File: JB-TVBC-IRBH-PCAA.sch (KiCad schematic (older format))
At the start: 11 parts, among them J1 CONN_2x20_FEM_100PITCH_635INS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, U1 CAT24C32

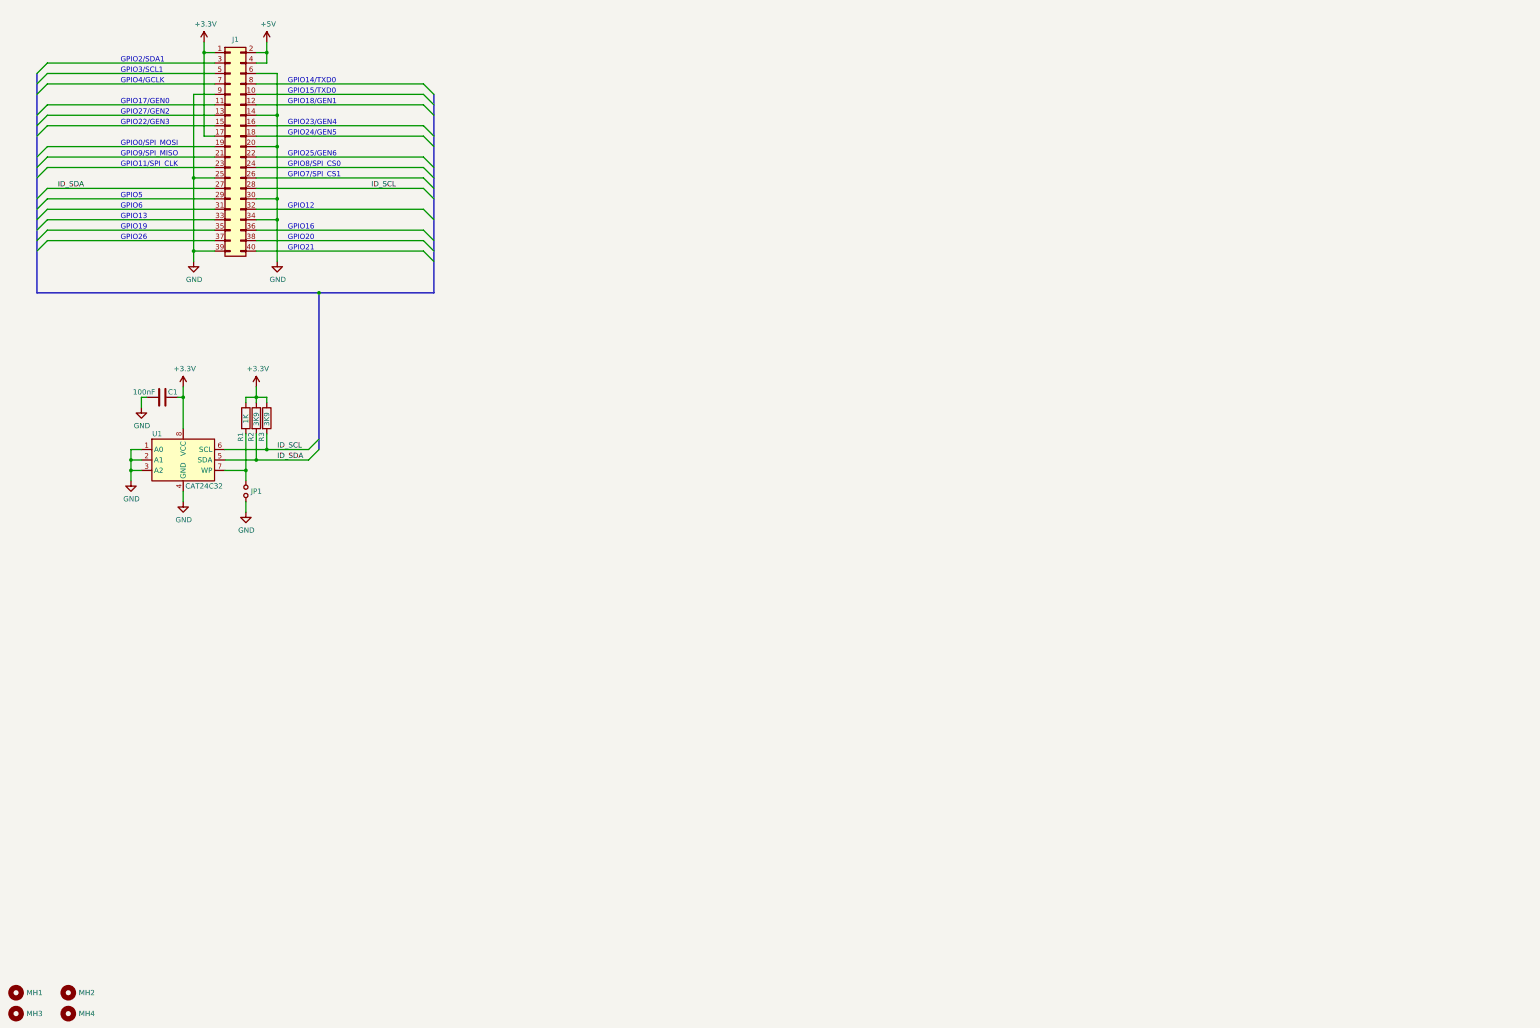
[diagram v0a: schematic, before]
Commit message: WIP. need to remove pull-up on PHASE and add pull-down on IN (gate driver
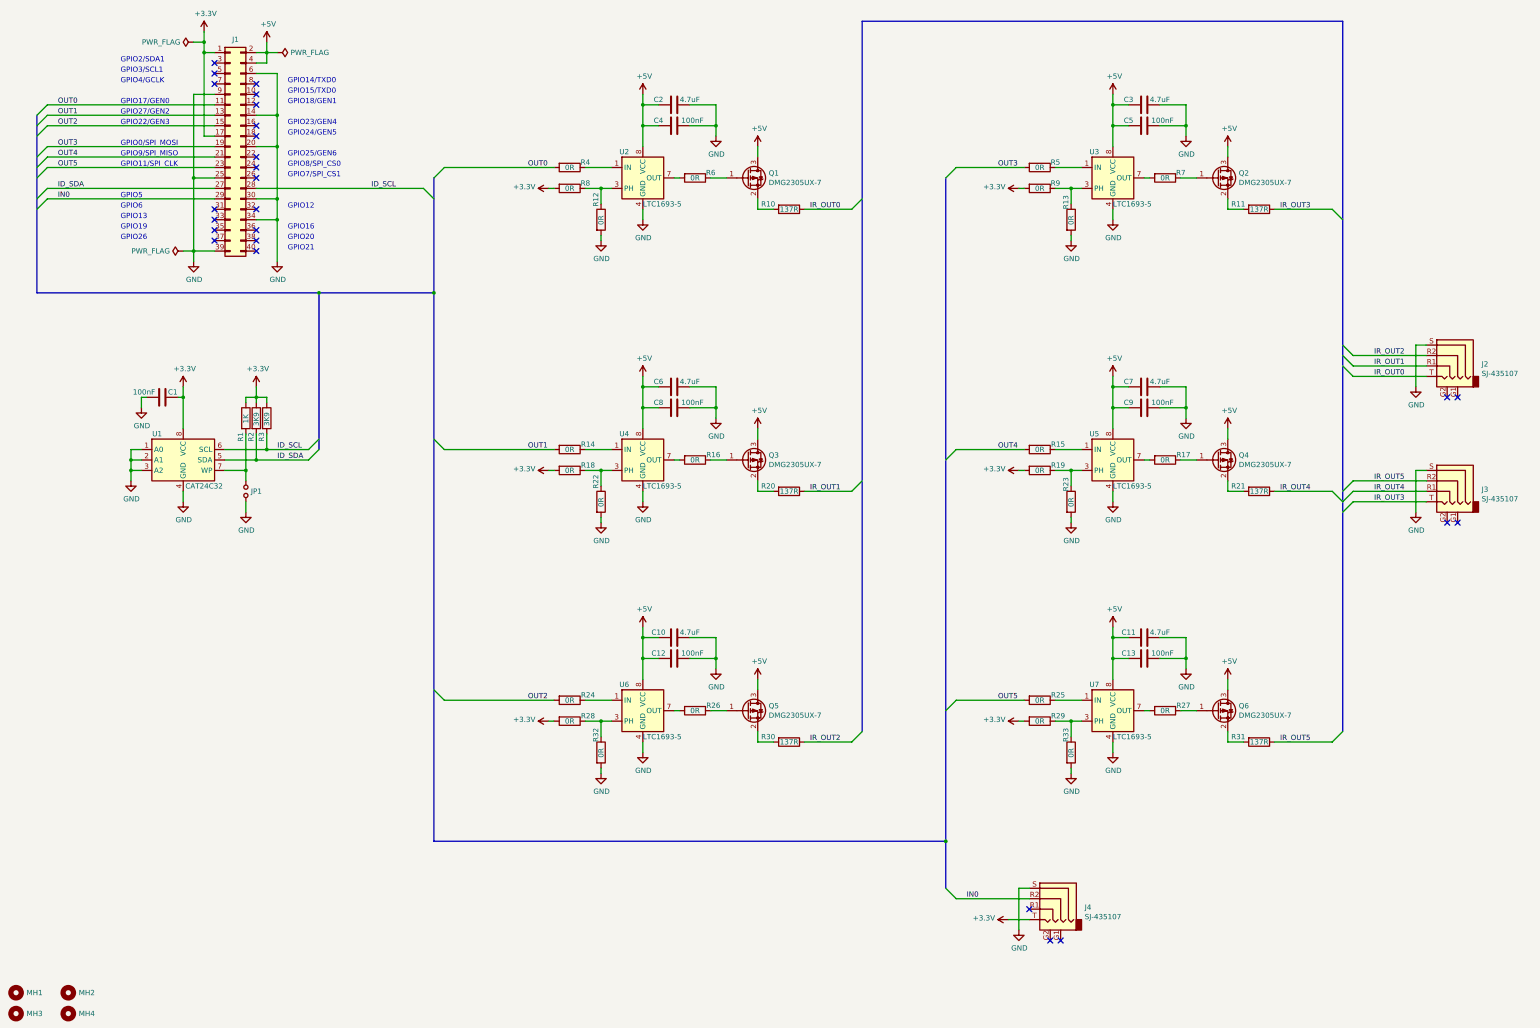
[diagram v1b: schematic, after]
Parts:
- removed C1: 100nF_0603_50V, Capacitor_SMD:C_0603_1608Metric_Pad1.05x0.95mm_HandSolder, symbol JB_Cap_Smd_50v:100nF_0603_50V
- added C1, C12, C13, C4, C5, C8, C9: 100nF_CER_0603_50V, Capacitor_SMD:C_0603_1608Metric_Pad1.05x0.95mm_HandSolder, symbol JB_Cap_Smd_50v:100nF_CER_0603_50V
- added C10, C11, C2, C3, C6, C7: 4.7uF_CER_0805_16V, Capacitor_SMD:C_0805_2012Metric_Pad1.15x1.40mm_HandSolder, symbol JB_Cap_Smd_16v:4.7uF_CER_0805_16V
- added J2, J3, J4: SJ-435107, JB_Connector_Barrel_Audio:SJ-435107, symbol JB_Connector_Barrel_Audio:SJ-435107
- added Q1, Q2, Q3, Q4, Q5, Q6: DMG2305UX-7, Package_TO_SOT_SMD:SOT-23_Handsoldering, symbol JB_Mosfet_P-Ch:DMG2305UX-7
- added R10, R11, R20, R21, R30, R31: 137R_1206_250MW, Resistor_SMD:R_1206_3216Metric_Pad1.42x1.75mm_HandSolder, symbol JB_Res_Smd_0w250:137R_1206_250MW
- added R12, R13, R14, R15, R16, R17, R18, R19, R22, R23, R24, R25, R26, R27, R28, R29, R32, R33, R4, R5, R6, R7, R8, R9: 0R_0603_100MW, Resistor_SMD:R_0603_1608Metric_Pad1.05x0.95mm_HandSolder, symbol JB_Res_Smd_0w100:0R_0603_100MW
- added U2, U3, U4, U5, U6, U7: LTC1693-5, Package_SO:MSOP-8_3x3mm_P0.65mm, symbol JB_Gate_Driver:LTC1693-5
- J1: Digi-Key PArt Number SAM9319-ND -> (none); Digi-Key Part Number (none) -> SAM9319-ND
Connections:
- net +3V3: now also C1.1, J4.T, R18.2, R19.2, R28.2, R29.2, R8.2, R9.2
- net +5V: now also C10.2, C11.2, C12.2, C13.2, C2.2, C3.2, C4.2, C5.2, C6.2, C7.2, C8.2, C9.2, Q1.3 (D), Q2.3 (D), Q3.3 (D), Q4.3 (D), Q5.3 (D), Q6.3 (D), U2.8 (VCC), U3.8 (VCC), U4.8 (VCC), U5.8 (VCC), U6.8 (VCC), U7.8 (VCC)
- net GND: now also C1.2, C10.1, C11.1, C12.1, C13.1, C2.1, C3.1, C4.1, C5.1, C6.1, C7.1, C8.1, C9.1, J2.S, J3.S, J4.S, R12.2, R13.2, R22.2, R23.2, R32.2, R33.2, U2.4 (GND), U3.4 (GND), U4.4 (GND), U5.4 (GND), U6.4 (GND), U7.4 (GND)
- net OUT0: now reaches J1.11 (Pin_11)
- net OUT0: now also R4.2
- net OUT1: now reaches J1.13 (Pin_13)
- net OUT1: now also R14.2
- net OUT2: now reaches J1.15 (Pin_15)
- net OUT2: now also R24.2
- net OUT3: now reaches J1.19 (Pin_19)
- net OUT3: now also R5.2
- net OUT4: now reaches J1.21 (Pin_21)
- net OUT4: now also R15.2
- net OUT5: now reaches J1.23 (Pin_23)
- net OUT5: now also R25.2
- net IN0: now reaches J1.29 (Pin_29)
- net IN0: now also J4.R2
- new net: R4.1, U2.1 (IN)
- new net: R12.1, R8.1, U2.3 (PH)
- new net: R6.2, U2.7 (OUT)
- new net: R14.1, U4.1 (IN)
- new net: R18.1, R22.1, U4.3 (PH)
- new net: R16.2, U4.7 (OUT)
- new net: R24.1, U6.1 (IN)
- new net: R28.1, R32.1, U6.3 (PH)
- new net: R26.2, U6.7 (OUT)
- new net: R5.1, U3.1 (IN)
- new net: R13.1, R9.1, U3.3 (PH)
- new net: R7.2, U3.7 (OUT)
- new net: R15.1, U5.1 (IN)
- new net: R19.1, R23.1, U5.3 (PH)
- new net: R17.2, U5.7 (OUT)
- new net: R25.1, U7.1 (IN)
- new net: R29.1, R33.1, U7.3 (PH)
- new net: R27.2, U7.7 (OUT)
- new net: Q1.1 (G), R6.1
- new net: Q2.1 (G), R7.1
- new net: Q4.1 (G), R17.1
- new net: Q6.1 (G), R27.1
- new net: Q5.1 (G), R26.1
- new net: Q3.1 (G), R16.1
- new net: Q1.2 (S), R10.2
- new net: Q2.2 (S), R11.2
- new net: Q4.2 (S), R21.2
- new net: Q3.2 (S), R20.2
- new net: Q5.2 (S), R30.2
- new net: Q6.2 (S), R31.2
- new net IR_OUT0: J2.T, R10.1
- new net IR_OUT1: J2.R1, R20.1
- new net IR_OUT2: J2.R2, R30.1
- new net IR_OUT3: J3.T, R11.1
- new net IR_OUT4: J3.R1, R21.1
- new net IR_OUT5: J3.R2, R31.1
- no-connect marks 0 -> 26

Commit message: adding fiducial + graphics symbol
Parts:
- added FID1, FID2, FID3, FID4, FID5, FID6, FID7, FID8: Fiducial, JB_Mechanical:Fiducial_1.5mm_Mask3mm, symbol JB_Mechanical:Fiducial
- added G1: JudeBake_Logo, JB_Bitmaps:JB_Logo_10MM, symbol JB_Bitmap:JudeBake_Logo
- added G2: CC-BY-SA_Logo, JB_Bitmaps:CC-BY-SA_10MM, symbol JB_Bitmap:CC-BY-SA_Logo
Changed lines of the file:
@@
 	0    1    1    0
+$EndComp
+$Comp
+L JB_Bitmap:JudeBake_Logo G1
+U 1 1 5E70CA7A
+P 15300 9000
+F 0 "G1" H 15300 8877 60  0001 C CNN
+F 1 "JudeBake_Logo" H 15300 9123 60  0001 C CNN
+F 2 "JB_Bitmaps:JB_Logo_10MM" H 15300 9000 50  0001 C CNN
+F 3 "" H 15300 9000 50  0001 C CNN
+	1    15300 9000
+	1    0    0    -1
+$EndComp
+$Comp
+L JB_Bitmap:CC-BY-SA_Logo G2
+U 1 1 5E70D851
+P 15800 9000
+F 0 "G2" H 15800 8955 60  0001 C CNN
+F 1 "CC-BY-SA_Logo" H 15800 9045 60  0001 C CNN
+F 2 "JB_Bitmaps:CC-BY-SA_10MM" H 15800 9000 50  0001 C CNN
+F 3 "" H 15800 9000 50  0001 C CNN
+	1    15800 9000
+	1    0    0    -1
+$EndComp
+$Comp
+L JB_Mechanical:Fiducial FID1
+U 1 1 5E715969
+P 1700 10200
+F 0 "FID1" H 1785 10200 50  0000 L CNN
+F 1 "Fiducial" H 1700 10325 50  0001 C CNN
+F 2 "JB_Mechanical:Fiducial_1.5mm_Mask3mm" H 1700 10200 50  0001 C CNN
+F 3 "~" H 1700 10200 50  0001 C CNN
+	1    1700 10200
+	1    0    0    -1
+$EndComp
+$Comp
+L JB_Mechanical:Fiducial FID3
+U 1 1 5E71703E
+P 1700 10400
+F 0 "FID3" H 1785 10400 50  0000 L CNN
+F 1 "Fiducial" H 1700 10525 50  0001 C CNN
+F 2 "JB_Mechanical:Fiducial_1.5mm_Mask3mm" H 1700 10400 50  0001 C CNN
+F 3 "~" H 1700 10400 50  0001 C CNN
+	1    1700 10400
+	1    0    0    -1
+$EndComp
+$Comp
+L JB_Mechanical:Fiducial FID4
+U 1 1 5E7179F8
+P 2200 10400
+F 0 "FID4" H 2285 10400 50  0000 L CNN
+F 1 "Fiducial" H 2200 10525 50  0001 C CNN
+F 2 "JB_Mechanical:Fiducial_1.5mm_Mask3mm" H 2200 10400 50  0001 C CNN
+F 3 "~" H 2200 10400 50  0001 C CNN
+	1    2200 10400
+	1    0    0    -1
+$EndComp
+$Comp
+L JB_Mechanical:Fiducial FID2
+U 1 1 5E7183BE
+P 2200 10200
+F 0 "FID2" H 2285 10200 50  0000 L CNN
+F 1 "Fiducial" H 2200 10325 50  0001 C CNN
+F 2 "JB_Mechanical:Fiducial_1.5mm_Mask3mm" H 2200 10200 50  0001 C CNN
+F 3 "~" H 2200 10200 50  0001 C CNN
+	1    2200 10200
+	1    0    0    -1
 $EndComp
 Wire Bus Line
@@
 Wire Bus Line
 	800  1800 800  3500
+$Comp
+L JB_Mechanical:Fiducial FID5
+U 1 1 5E7278A2
+P 2700 10200
+F 0 "FID5" H 2785 10200 50  0000 L CNN
+F 1 "Fiducial" H 2700 10325 50  0001 C CNN
+F 2 "JB_Mechanical:Fiducial_1.5mm_Mask3mm" H 2700 10200 50  0001 C CNN
+F 3 "~" H 2700 10200 50  0001 C CNN
+	1    2700 10200
+	1    0    0    -1
+$EndComp
+$Comp
+L JB_Mechanical:Fiducial FID7
+U 1 1 5E728579
+P 2700 10400
+F 0 "FID7" H 2785 10400 50  0000 L CNN
+F 1 "Fiducial" H 2700 10525 50  0001 C CNN
+F 2 "JB_Mechanical:Fiducial_1.5mm_Mask3mm" H 2700 10400 50  0001 C CNN
+F 3 "~" H 2700 10400 50  0001 C CNN
+	1    2700 10400
+	1    0    0    -1
+$EndComp
+$Comp
+L JB_Mechanical:Fiducial FID6
+U 1 1 5E728F5C
+P 3100 10200
+F 0 "FID6" H 3185 10200 50  0000 L CNN
+F 1 "Fiducial" H 3100 10325 50  0001 C CNN
+F 2 "JB_Mechanical:Fiducial_1.5mm_Mask3mm" H 3100 10200 50  0001 C CNN
+F 3 "~" H 3100 10200 50  0001 C CNN
+	1    3100 10200
+	1    0    0    -1
+$EndComp
+$Comp
+L JB_Mechanical:Fiducial FID8
+U 1 1 5E72994B
+P 3100 10400
+F 0 "FID8" H 3185 10400 50  0000 L CNN
+F 1 "Fiducial" H 3100 10525 50  0001 C CNN
+F 2 "JB_Mechanical:Fiducial_1.5mm_Mask3mm" H 3100 10400 50  0001 C CNN
+F 3 "~" H 3100 10400 50  0001 C CNN
+	1    3100 10400
+	1    0    0    -1
+$EndComp
 $EndSCHEMATC
